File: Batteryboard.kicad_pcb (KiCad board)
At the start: 4 copper layers, 76.2 x 76.2 mm, 147 parts, among them IC1 FAN4010IL6X_F113, IC2 FAN4010IL6X_F113, IC3 FAN4010IL6X_F113, J1 Conn_01x02_Male, J2 Conn_01x03_Male, J3 Conn_01x05_Male, J4 Conn_01x02_Male, J5 SC_19-20, Q1 SI7617DN-T1-GE3, Q2 SI7617DN-T1-GE3, Q3 SI7617DN-T1-GE3, Q4 SIS412DN-T1-GE3, Q5 SIS412DN-T1-GE3, Q6 SIS412DN-T1-GE3, Q7 SI7617DN-T1-GE3, Q8 SIS412DN-T1-GE3, U1 BQ24617RGET, U2 TPS65279DAPR, U3 BQ29200DRBT, U4 PIC18F25K50-I_SO, U5 MCP2515-xSO, U6 SN65HVD1050D

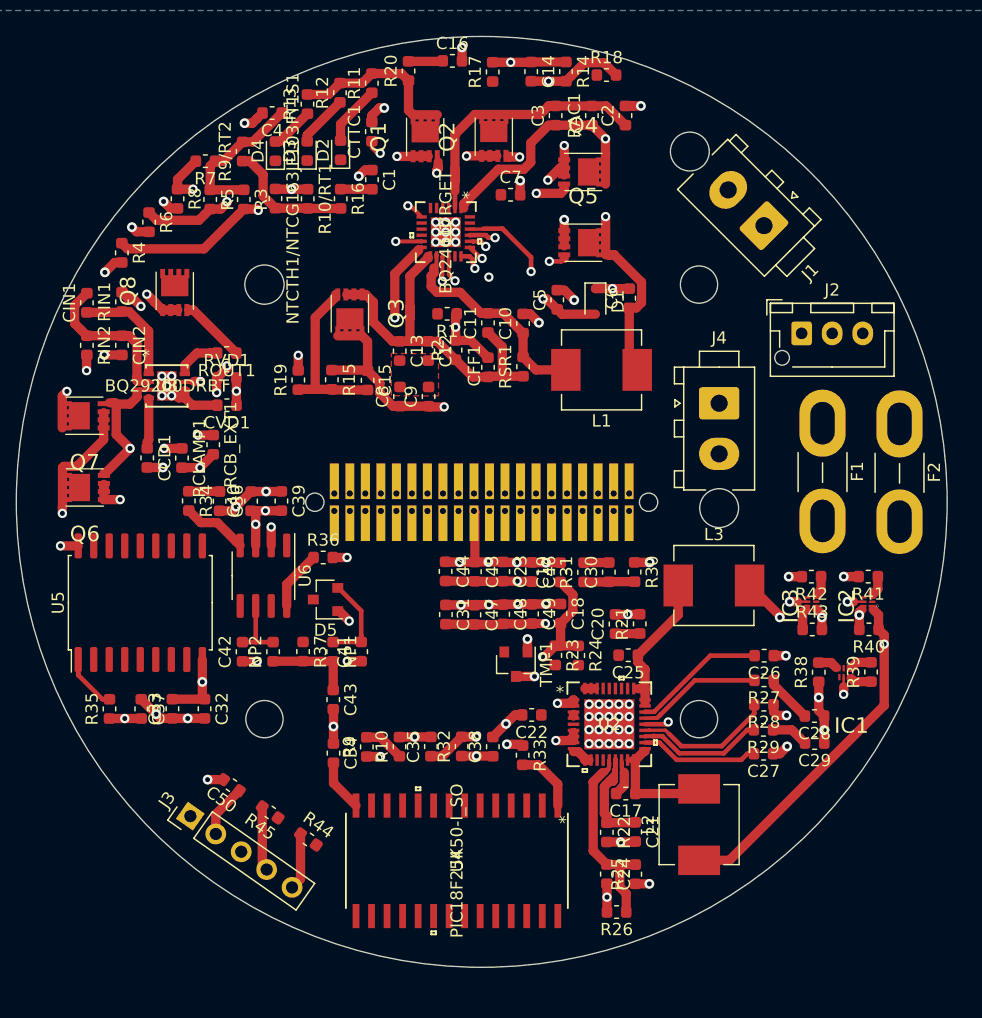
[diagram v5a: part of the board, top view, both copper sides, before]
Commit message: finished rotuing all my traces, grounding next
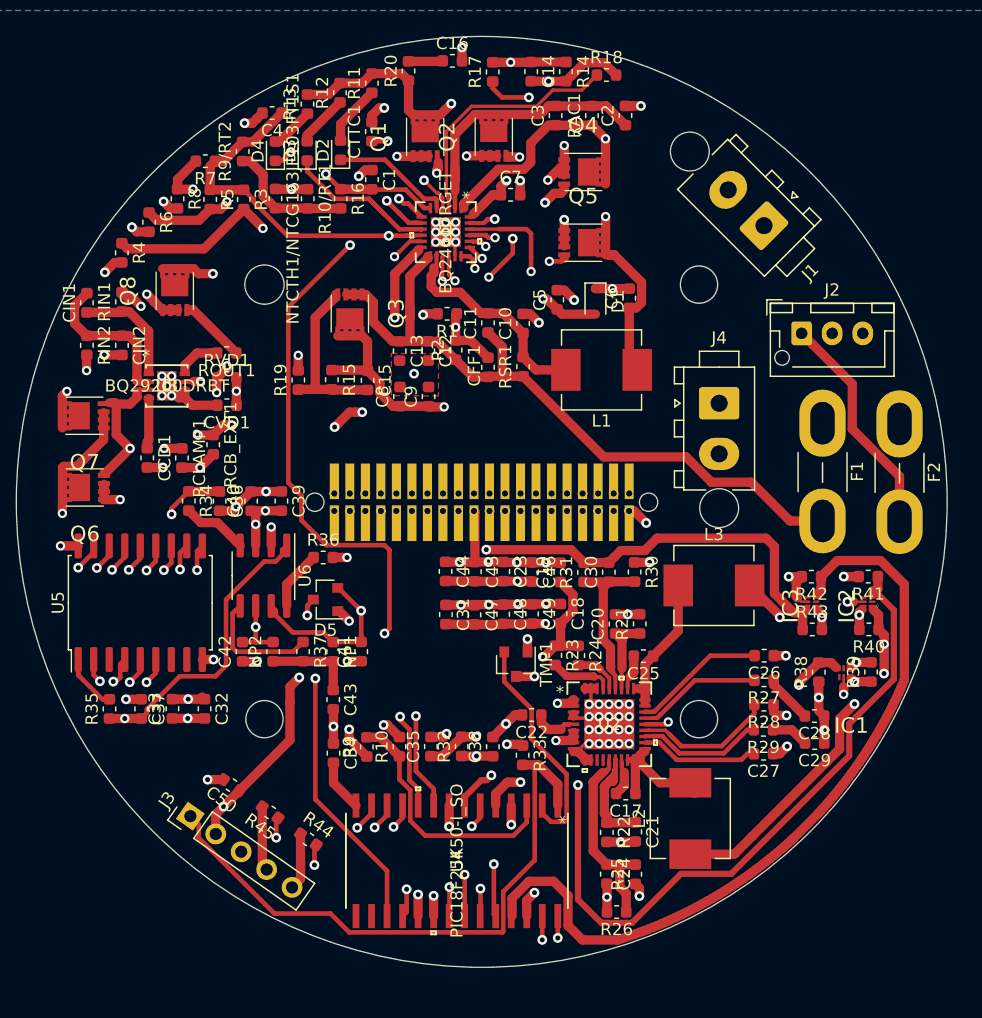
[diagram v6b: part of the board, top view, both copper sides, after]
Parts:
- moved C25 1.25 mm to (248.6, 75.7)
- moved L2 0.88 mm to (252.5, 89.0)
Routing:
- net 3V3: track 8.80 -> 129.3 mm, vias 0 -> 8
- net TS: track 2.56 -> 85.7 mm, vias 0 -> 4
- net Q6S: track 29.8 -> 107.9 mm
- net Net-(F2-Pad1): track 0.00 -> 70.3 mm, vias 0 -> 1
- net 5VCURRENT: track 2.44 -> 67.9 mm, vias 0 -> 2
- net 3V3CURRENT: track 2.45 -> 65.2 mm
- net CS: track 0.00 -> 62.4 mm, vias 0 -> 2
- net SCK: track 0.00 -> 61.6 mm, vias 0 -> 2
- net INT: track 0.00 -> 61.2 mm, vias 0 -> 2
- net SO: track 0.00 -> 59.9 mm, vias 0 -> 2
- net SI: track 0.00 -> 58.8 mm, vias 0 -> 2
- net Net-(J2-Pad2): track 13.8 -> 70.6 mm, vias 2 -> 5
- net Q4D: track 69.5 -> 125.0 mm, vias 2 -> 3
- net RESET: track 0.00 -> 52.4 mm, vias 0 -> 2
- net MCLR: track 5.28 -> 50.3 mm
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
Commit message: grounded everything, hopefully well, but that is not a guarantee
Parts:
- moved C22 7.00 mm to (232.6, 79.4)
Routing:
- net PGND2: track 133.5 -> 147.4 mm, vias 93 -> 94
- net V7V: track 4.17 -> 12.4 mm, vias 0 -> 2
- net Net-(C7-Pad1): track 36.8 -> 34.5 mm
- net CAN_H: track 32.6 -> 33.6 mm

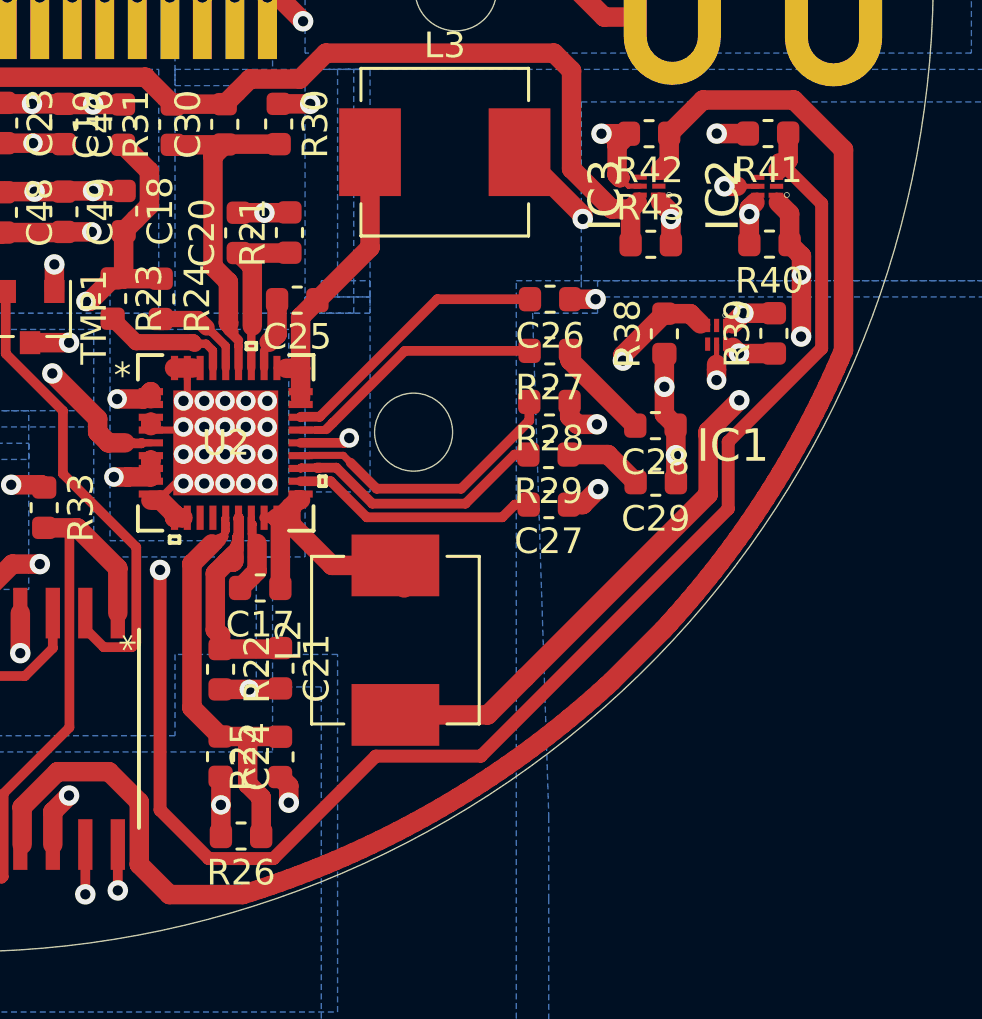
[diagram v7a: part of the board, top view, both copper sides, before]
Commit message: fixed current sense ICs
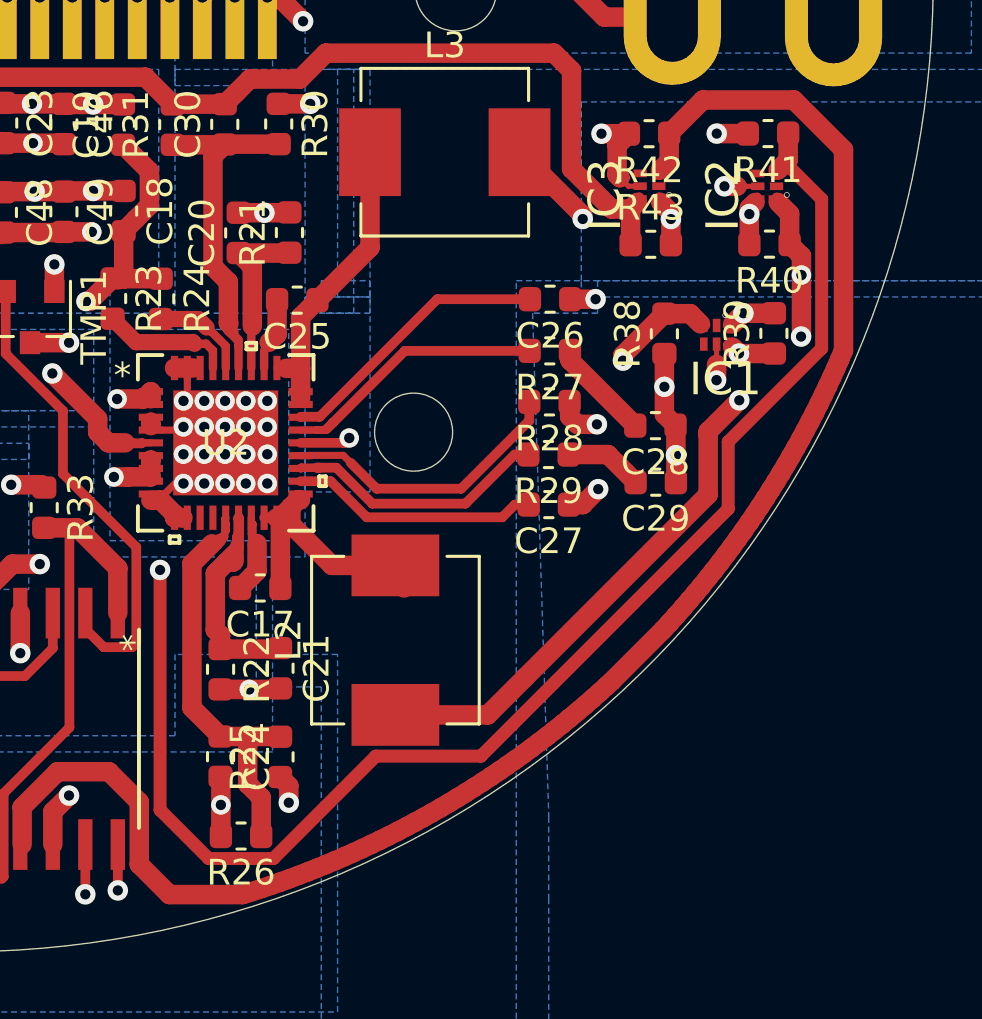
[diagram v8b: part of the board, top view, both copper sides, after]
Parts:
- IC1, IC2, IC3: footprint FAN4010IL6X_F113:6-LEAD_MICROPAK -> MASA-LIB:6-LEAD_MICROPAK
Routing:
- net 5VCURRENT: track 67.9 -> 67.2 mm
